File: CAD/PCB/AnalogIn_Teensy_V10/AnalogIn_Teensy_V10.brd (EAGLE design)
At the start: 93.2 x 73.5 mm, 97 parts, among them IC1 AD8599R, IC2 AD8599R, IC3 AD8599R, IC4 AD8599R, U1 AD7327BRUZ, U2 SN65HVD31DR, U3 SN65HVD31DR

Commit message: Update TeensyV10 board
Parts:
- removed C1, C2, C3: 4.7uf, SparkFun-Capacitors:1206
- removed R4: 22, SparkFun-Resistors:1206
- added C41, C42, C43, C44, C45, C46, C47, C48: (no value), SparkFun-Capacitors:0603-CAP
- added C49: 10uf, SparkFun-Capacitors:0603-CAP
- added C50, C51: 0.1uf, SparkFun-Capacitors:0603-CAP
- added R29, R31, R32, R33, R34, R35, R36: (no value), SparkFun-Resistors:0603-RES
- added R30: 50, SparkFun-Resistors:0603-RES
- added R37: 22, SparkFun-Resistors:0603-RES
- C13, C14: value 0.1uf -> 4.7uf; device SparkFun-Capacitors:1206 -> SparkFun-Capacitors:0603-CAP
- C4, C5, C6: device SparkFun-Capacitors:1206 -> SparkFun-Capacitors:0603-CAP
- C7: value 10uf -> 4.7uf; device SparkFun-Capacitors:1206 -> SparkFun-Capacitors:0603-CAP
- C8: value 680nf -> 680nF; device SparkFun-Capacitors:1206 -> SparkFun-Capacitors:0603-CAP
- R1, R11, R12, R14, R16, R17, R18, R2, R20, R21, R23, R24, R26, R27, R3, R6, R8, R9: device SparkFun-Resistors:1206 -> SparkFun-Resistors:0603-RES
- R10, R13, R15, R19, R22, R25, R28, R7: value 50 -> 180; device SparkFun-Resistors:1206 -> SparkFun-Resistors:0603-RES
- R5: value 50 -> (none); device SparkFun-Resistors:1206 -> SparkFun-Resistors:0603-RES
- moved C33 132.0 mm to (12.1, 40.6), turned to 180 degrees
- moved C32 131.8 mm to (12.1, 43.5), turned to 180 degrees
- moved C34 131.1 mm to (26.6, 38.5), turned to 90 degrees
- moved C29 128.5 mm to (26.6, 43.9), turned to 270 degrees
- moved C31 127.9 mm to (22.9, 42.5)
- moved C30 124.9 mm to (22.9, 40.0)
- moved R17 121.4 mm to (11.9, 47.0)
- moved R18 120.7 mm to (19.4, 46.5)
- moved IC3 119.9 mm to (17.9, 40.9), turned to 180 degrees
- moved C39 119.0 mm to (11.8, 27.1), turned to 180 degrees
- moved R19 119.0 mm to (22.8, 44.8)
- moved C35 118.7 mm to (25.6, 26.9), turned to 270 degrees
- moved R23 117.7 mm to (11.9, 30.6)
- moved C36 116.5 mm to (22.4, 25.6)
- moved R26 116.1 mm to (18.9, 29.7)
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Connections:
- net +V12 renamed +VOUT
- net -V12 renamed -VOUT
- removed net N$18: C12.1, C19.1, IC1.8
- removed net N$19: C20.1, C21.1, IC1.4
- removed net N$26: C24.1, C25.1, IC2.8
- removed net N$27: C26.1, C27.1, IC2.4
- removed net N$34: C30.1, C31.1, IC3.8
- removed net N$35: C32.1, C33.1, IC3.4
- removed net N$42: C36.1, C37.1, IC4.8
- removed net N$43: C38.1, C39.1, IC4.4
- net ADC_CS: now also R3.1; no longer R4.1
- net AGND: now also C41.2, C42.2, C43.2, C44.2, C45.2, C46.2, C47.2, C48.2, C49.2, C50.2, C51.2, C8.1, C9.2, R29.1, R31.1, R32.1, R33.1, R34.1, R35.1, R36.1, R5.1; no longer C13.2, C14.2, C7.2, C8.2
- net AIN0: now also R30.1; no longer R5.1
- net AIN7: now also R24.1; no longer R26.1
- net DGND: now also C13.1, C14.2, C7.2; no longer C1.2, C2.1, C3.2
- net MISO: now also R1.1; no longer R2.1
- net MOSI: now also R37.1; no longer R1.1
- net N$10: now also R37.2; no longer R1.2
- net N$11: now also R1.2; no longer R2.2
- net N$12: now also C14.1; no longer C1.1
- net N$13: now also R3.2; no longer R4.2
- net N$14: now also C41.1, R30.2; no longer R5.2
- net N$15: now also R2.2; no longer R3.2
- net N$16: now also R5.2
- net N$20: now also C42.1
- net N$21: now also R29.2
- net N$23: now also C43.1
- net N$24: now also R31.2
- net N$28: now also C44.1
- net N$29: now also R16.1, R32.2; no longer R15.1
- net N$30: now also R15.1, R16.2; no longer R15.2, R16.1
- net N$31: now also C45.1
- net N$32: now also R33.2
- net N$36: now also C46.1
- net N$37: now also R34.2
- net N$39: now also C47.1
- net N$40: now also R26.1, R35.2; no longer R24.1
- net N$41: now also R26.2; no longer R24.2
- net N$44: now also C48.1, R24.2; no longer R26.2
- net N$45: now also R36.2
- net REF: now also C8.2; no longer C8.1
- net SCLK: now also R2.1; no longer R3.1
- net V+12: now also C12.1, C19.1, C24.1, C25.1, C30.1, C31.1, C36.1, C37.1, C7.1, IC1.8, IC2.8, IC3.8, IC4.8; no longer C3.1
- net V-12: now also C13.2, C20.1, C21.1, C26.1, C27.1, C32.1, C33.1, C38.1, C39.1, C49.1, C50.1, IC1.4, IC2.4, IC3.4, IC4.4; no longer C2.2, C6.1, C7.1
- net V3IN: now also R15.2; no longer R16.2
- net VDD: now also C6.1; no longer C13.1
- net VSS: now also C51.1; no longer C14.1
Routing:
- net MISO: track 0.00 -> 68.5 mm, vias 0 -> 2
- net MOSI: track 0.00 -> 64.4 mm
- net -VOUT: track 0.00 -> 22.1 mm
- net AGND: track 31.3 -> 20.8 mm, vias 9 -> 8
- net N$12: track 0.00 -> 10.3 mm
- net +VOUT: track 0.00 -> 9.74 mm
- net VDD: track 16.8 -> 9.36 mm
- net VSS: track 15.8 -> 8.65 mm
- net V-12: track 11.0 -> 16.9 mm, vias 1 -> 2
- net DGND: track 17.4 -> 23.2 mm, vias 7 -> 10
- net V5: track 13.5 -> 17.4 mm, vias 2 -> 3
- net N$15: track 2.89 -> 6.65 mm
- net REF: track 10.1 -> 6.48 mm
- net SCLK: track 10.7 -> 7.66 mm
- net ADC_CS: track 14.3 -> 11.6 mm
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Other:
- board size 93.2 x 73.5 mm -> 95 x 76 mm

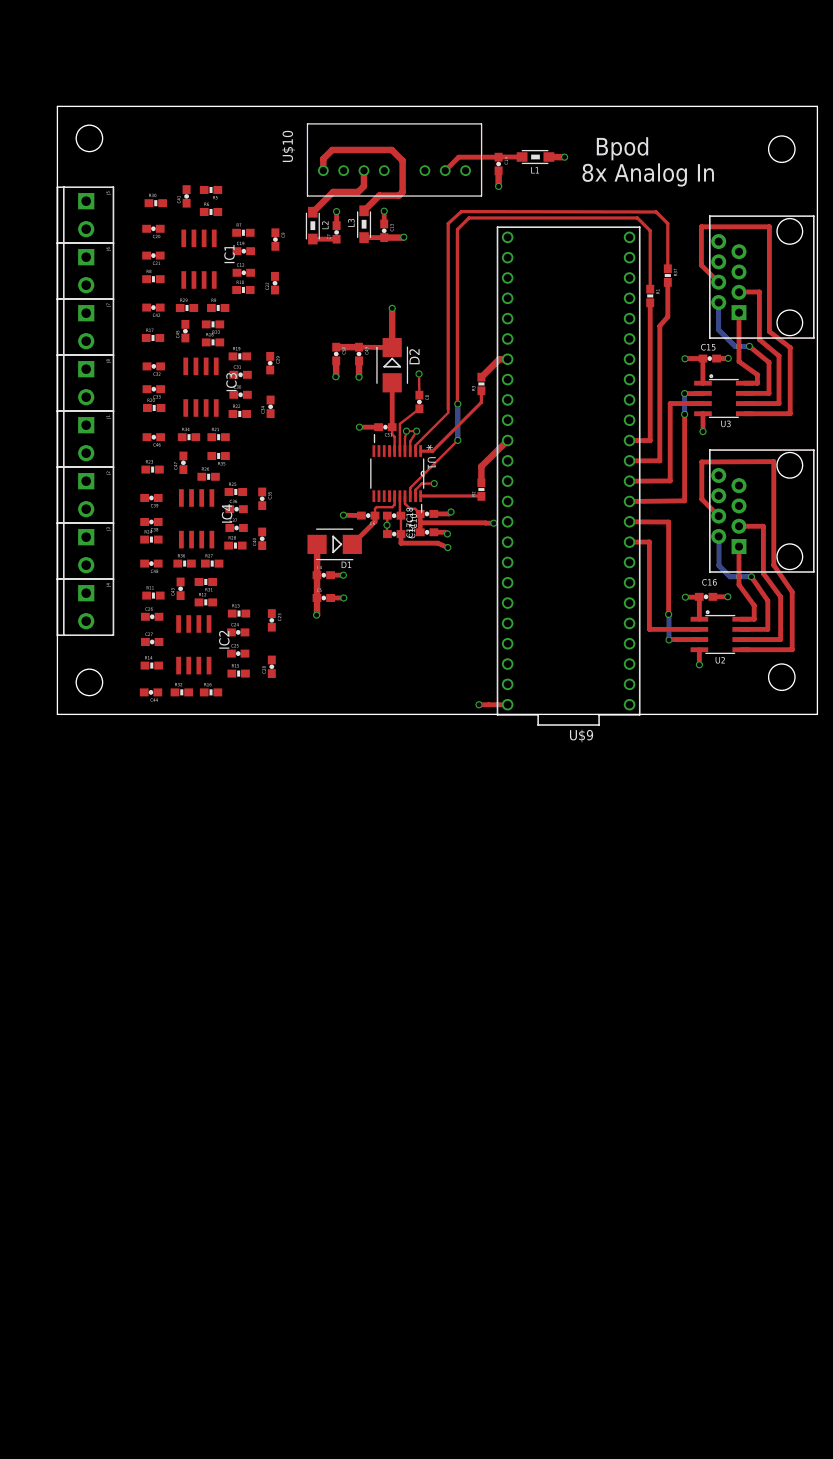
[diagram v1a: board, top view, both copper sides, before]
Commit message: Update Teensy verion
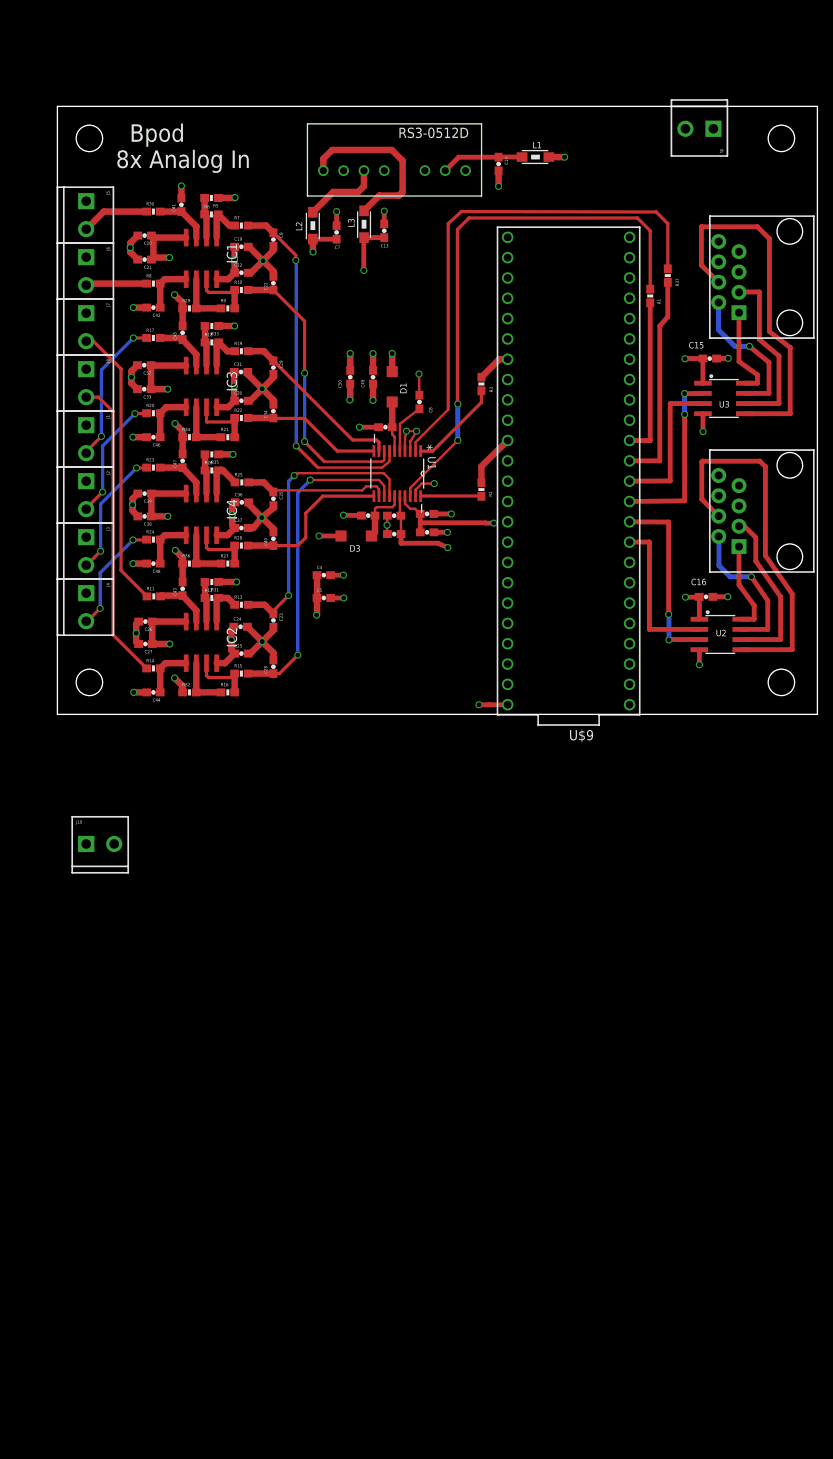
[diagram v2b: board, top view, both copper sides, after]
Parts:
- removed D2: (no value), diode:SMB
- added D3: MBR0520LT, diode:SOD123
- added J10, J9: (no value), SparkFun-Connectors:SCREWTERMINAL-3.5MM-2
- D1: value (none) -> MBR0520LT; device diode:SMB -> diode:SOD123
- moved D1 21.0 mm to (41.9, 41.0), turned to 270 degrees
- moved C49 3.39 mm to (39.5, 42.1)
- moved C50 3.39 mm to (36.6, 42.1)
- moved R16 2.10 mm to (21.3, 2.75)
- moved R27 1.95 mm to (21.3, 18.9)
- moved R25 1.42 mm to (23.1, 29.0)
- moved C35 1.40 mm to (27.0, 26.9)
- moved C40 1.40 mm to (27.0, 21.9)
- moved C20 1.39 mm to (10.9, 59.9)
- moved U$8 1.35 mm to (90.5, 72.0)
- moved C41 1.23 mm to (15.5, 63.7)
- moved C32 1.21 mm to (10.8, 43.6)
- moved C21 1.21 mm to (10.9, 56.9)
- moved R9 1.20 mm to (21.3, 50.8)
- moved C33 1.20 mm to (10.8, 40.6)
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- renumbered U$10 to RS3-0512D
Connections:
- new net N$18: J9.2, U$9.31/A12
- new net N$19: J10.2, U$9.32/A13
- net DGND: now also J10.1, J9.1
- net V+12: now also D3.A; no longer D1.A
- net V-12: now also D1.C; no longer D2.C
- net VDD: now also D3.C; no longer D1.C
- net VSS: now also D1.A; no longer D2.A
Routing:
- net AGND: track 20.8 -> 106.1 mm, vias 8 -> 29
- net V0IN: track 0.00 -> 45.7 mm, vias 0 -> 2
- net V3IN: track 0.00 -> 40.5 mm, vias 0 -> 2
- net AIN3: track 0.00 -> 37.9 mm
- net V2IN: track 0.00 -> 36.4 mm, vias 0 -> 2
- net V1IN: track 0.00 -> 35.9 mm, vias 0 -> 2
- net AIN2: track 0.00 -> 35.6 mm
- net V-12: track 16.9 -> 50.4 mm, vias 2 -> 8
- net V+12: track 11.9 -> 36.9 mm, vias 1 -> 7
- net V4IN: track 0.00 -> 22.2 mm
- net V7IN: track 0.00 -> 20.1 mm
- net AIN4: track 0.00 -> 18.5 mm, vias 0 -> 2
- net V6IN: track 0.00 -> 18.1 mm
- net V5IN: track 0.00 -> 17.4 mm
- net AIN6: track 0.00 -> 16.1 mm, vias 0 -> 2
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
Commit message: Teensy board
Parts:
- moved J9 83.5 mm to (37.0, 2.80), turned to 0 degrees
- moved J10 44.7 mm to (44.0, 2.80)
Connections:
- net N$18: now also J10.2, U$9.23/A9; no longer J9.2, U$9.31/A12
- net N$19: now also J9.2, U$9.22/A8; no longer J10.2, U$9.32/A13
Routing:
- net N$19: track 0.00 -> 22.5 mm
- net N$18: track 0.00 -> 13.9 mm
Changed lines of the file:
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@@
 <layers>
 <layer number="1" name="Top" color="4" fill="1" visible="yes" active="yes"/>
-<layer number="2" name="Route2" color="1" fill="3" visible="no" active="yes"/>
+<layer number="2" name="Route2" color="1" fill="3" visible="yes" active="yes"/>
 <layer number="3" name="Route3" color="4" fill="3" visible="no" active="no"/>
 <layer number="4" name="Route4" color="1" fill="4" visible="no" active="no"/>
@@
 <layer number="13" name="Route13" color="4" fill="5" visible="no" active="no"/>
 <layer number="14" name="Route14" color="1" fill="6" visible="no" active="no"/>
-<layer number="15" name="Route15" color="58" fill="6" visible="no" active="yes"/>
+<layer number="15" name="Route15" color="58" fill="6" visible="yes" active="yes"/>
 <layer number="16" name="Bottom" color="1" fill="1" visible="yes" active="yes"/>
 <layer number="17" name="Pads" color="2" fill="1" visible="yes" active="yes"/>
@@
 <layer number="27" name="tValues" color="7" fill="1" visible="yes" active="yes"/>
 <layer number="28" name="bValues" color="7" fill="1" visible="yes" active="yes"/>
-<layer number="29" name="tStop" color="7" fill="3" visible="yes" active="yes"/>
-<layer number="30" name="bStop" color="7" fill="6" visible="yes" active="yes"/>
+<layer number="29" name="tStop" color="7" fill="3" visible="no" active="yes"/>
+<layer number="30" name="bStop" color="7" fill="6" visible="no" active="yes"/>
 <layer number="31" name="tCream" color="7" fill="4" visible="yes" active="yes"/>
 <layer number="32" name="bCream" color="7" fill="5" visible="yes" active="yes"/>
@@
 <attribute name="NAME" x="43.65" y="40.05" size="0.8128" layer="25" rot="R90"/>
 </element>
-<element name="J9" library="SparkFun-Connectors" package="SCREWTERMINAL-3.5MM-2" value="" x="82" y="73.2" rot="R180">
-<attribute name="PROD_ID" value="CONN-08399" x="82" y="73.2" size="1.778" layer="27" rot="R180" display="off"/>
-</element>
-<element name="J10" library="SparkFun-Connectors" package="SCREWTERMINAL-3.5MM-2" value="" x="3.6" y="-16.2">
-<attribute name="PROD_ID" value="CONN-08399" x="3.6" y="-16.2" size="1.778" layer="27" display="off"/>
+<element name="J9" library="SparkFun-Connectors" package="SCREWTERMINAL-3.5MM-2" value="" x="37.05" y="2.8">
+<attribute name="PROD_ID" value="CONN-08399" x="37.05" y="2.8" size="1.778" layer="27" display="off"/>
+</element>
+<element name="J10" library="SparkFun-Connectors" package="SCREWTERMINAL-3.5MM-2" value="" x="44.05" y="2.8">
+<attribute name="PROD_ID" value="CONN-08399" x="44.05" y="2.8" size="1.778" layer="27" display="off"/>
 </element>
 </elements>
@@
 <wire x1="47.06" y1="22.76" x2="48.54" y2="22.76" width="0.6096" layer="1"/>
 <wire x1="48.54" y1="22.76" x2="48.75" y2="22.75" width="0.6096" layer="1"/>
+<contactref element="J10" pad="1"/>
 <contactref element="J9" pad="1"/>
-<contactref element="J10" pad="1"/>
-<wire x1="47.06" y1="22.76" x2="3.6" y2="-16.2" width="0" layer="19" extent="1-1"/>
 </signal>
 <signal name="N$2">
@@
 </signal>
 <signal name="N$18">
-<contactref element="U$9" pad="31/A12"/>
+<contactref element="J10" pad="2"/>
+<contactref element="U$9" pad="23/A9"/>
+<wire x1="56.28" y1="8.83" x2="48.98" y2="8.83" width="0.6096" layer="1"/>
+<wire x1="48.98" y1="8.83" x2="47.55" y2="7.4" width="0.6096" layer="1"/>
+<wire x1="47.55" y1="7.4" x2="47.55" y2="2.8" width="0.6096" layer="1"/>
+</signal>
+<signal name="N$19">
 <contactref element="J9" pad="2"/>
-<wire x1="71.52" y1="57.09" x2="78.5" y2="73.2" width="0" layer="19" extent="1-1"/>
-</signal>
-<signal name="N$19">
-<contactref element="U$9" pad="32/A13"/>
-<contactref element="J10" pad="2"/>
-<wire x1="7.1" y1="-16.2" x2="71.52" y2="59.63" width="0" layer="19" extent="1-1"/>
+<contactref element="U$9" pad="22/A8"/>
+<wire x1="56.28" y1="11.37" x2="43.67" y2="11.37" width="0.6096" layer="1"/>
+<wire x1="43.67" y1="11.37" x2="40.55" y2="8.25" width="0.6096" layer="1"/>
+<wire x1="40.55" y1="8.25" x2="40.55" y2="2.8" width="0.6096" layer="1"/>
 </signal>
 </signals>
